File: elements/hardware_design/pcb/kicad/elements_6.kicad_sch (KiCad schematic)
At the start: 19 parts

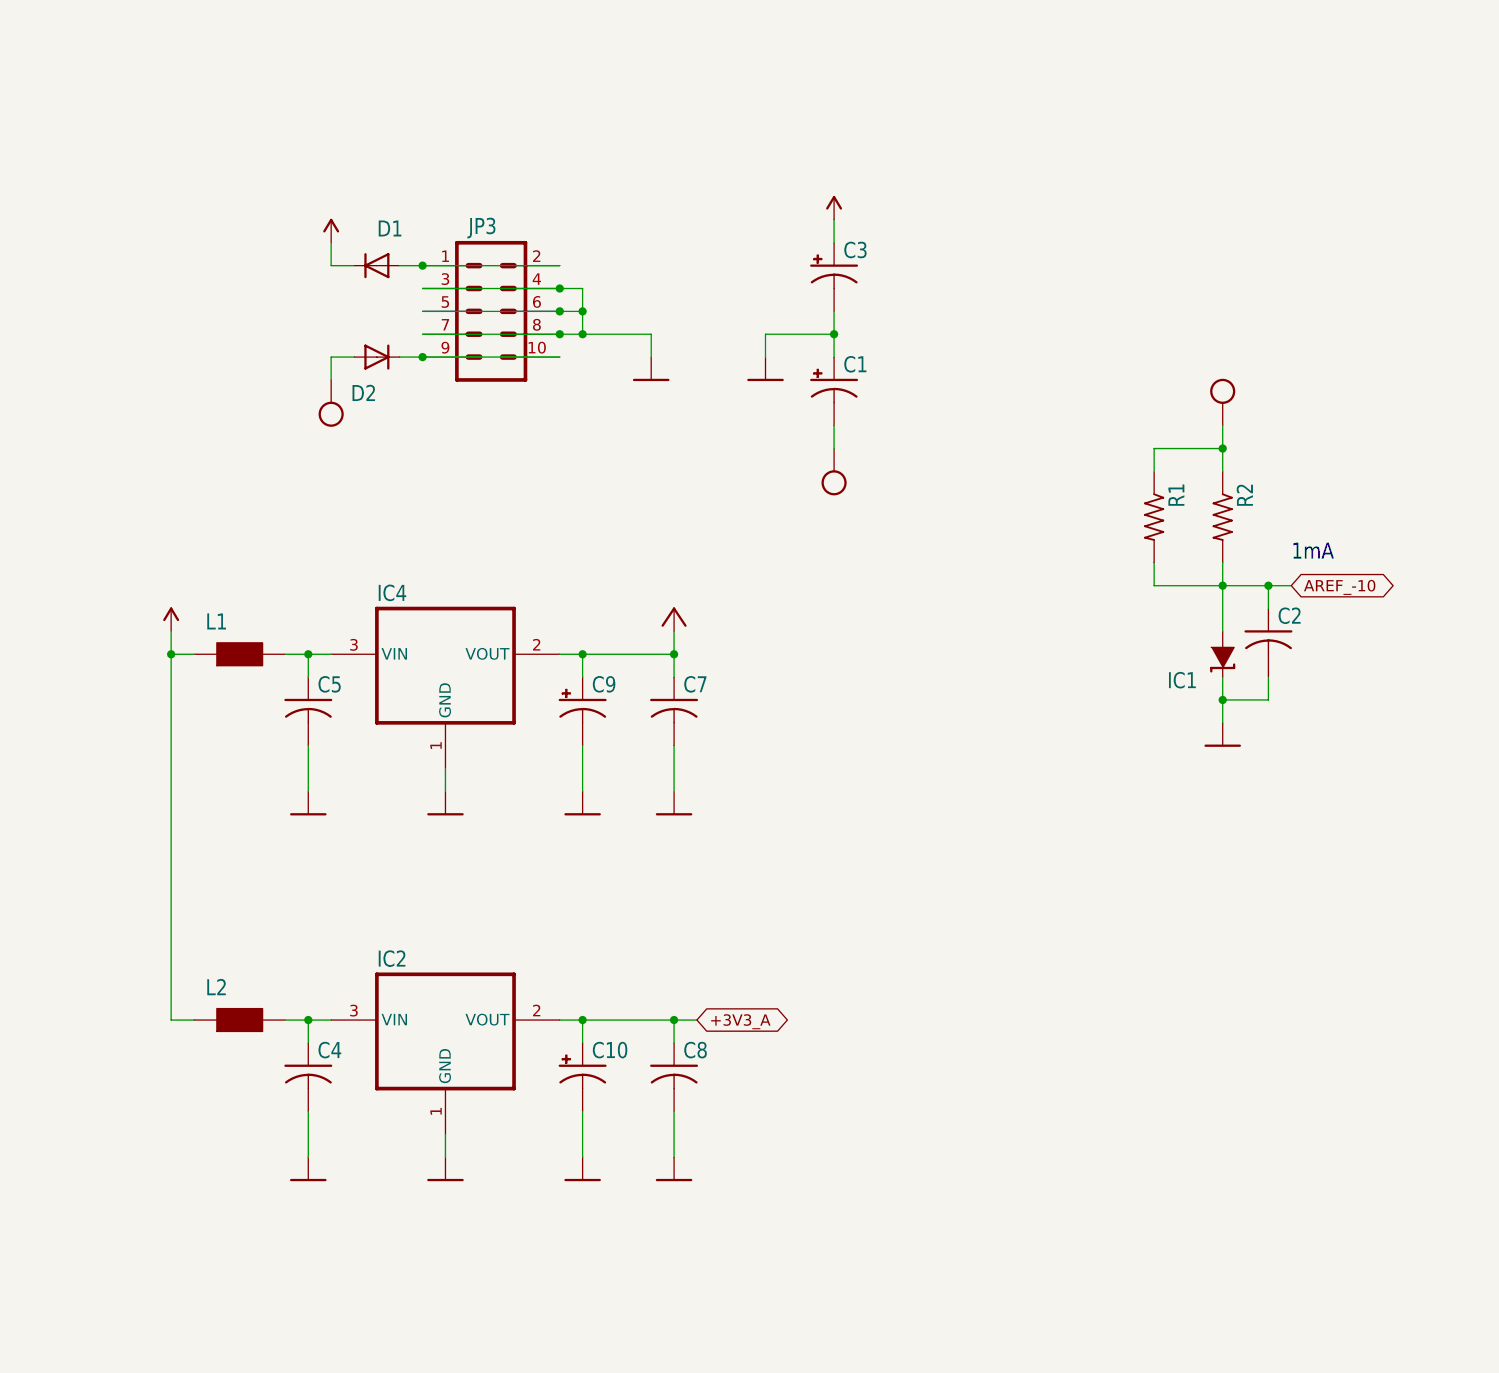
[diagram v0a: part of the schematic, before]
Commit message: swap wm8731 package (haven't drawn traces yet)
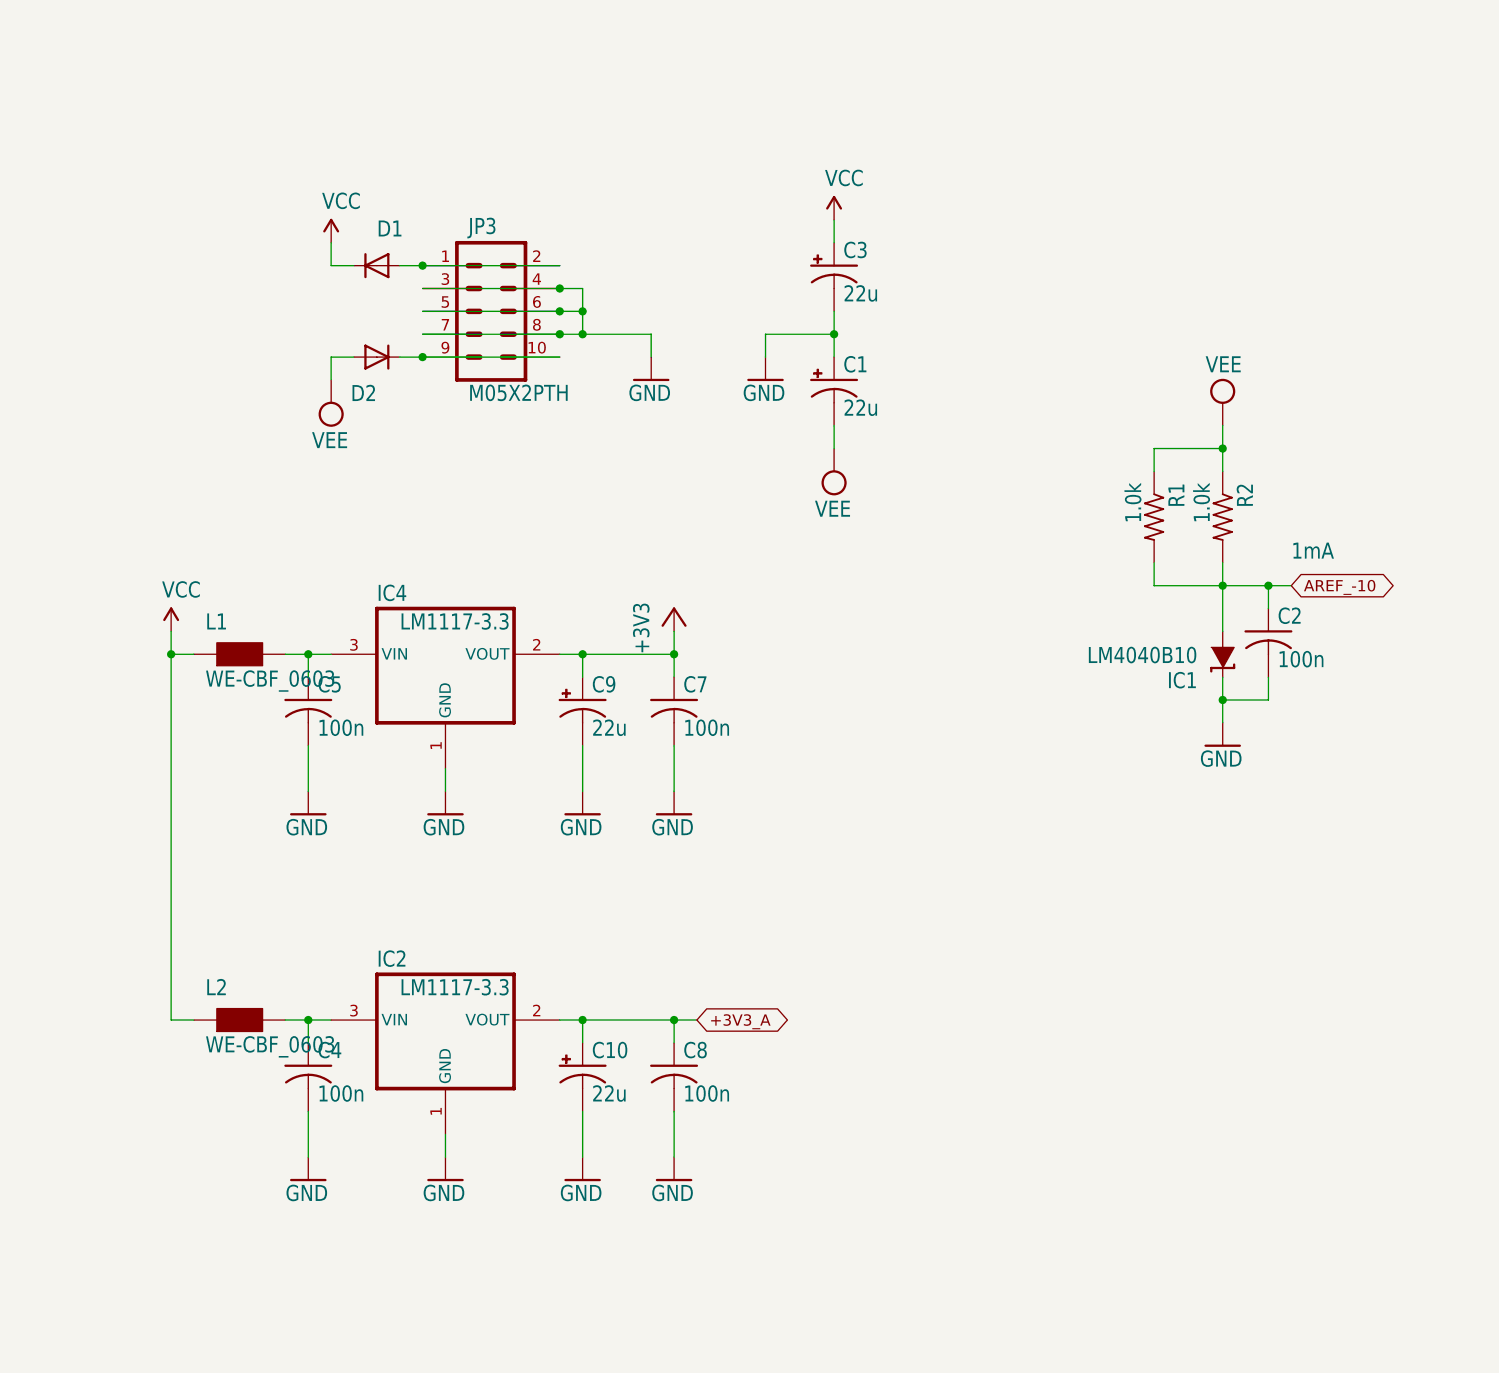
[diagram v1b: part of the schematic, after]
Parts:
- C1, C10, C3, C9: value (none) -> 22u; footprint (none) -> elements:PANASONIC_C
- C2, C4, C5, C7, C8: value (none) -> 100n; footprint (none) -> elements:C0603
- D1, D2: value (none) -> 1N5819HW; footprint (none) -> elements:SOD123
- IC1: value (none) -> LM4040B10; footprint (none) -> elements:DBZ_R-PDSO-G3
- IC2, IC4: value (none) -> LM1117-3.3; footprint (none) -> elements:SOT223
- JP3: value (none) -> M05X2PTH; footprint (none) -> elements:AVR_ICSP
- L1, L2: value (none) -> WE-CBF_0603; footprint (none) -> elements:0603
- R1, R2: value (none) -> 1.0k; footprint (none) -> elements:R0603

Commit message: add optional SMD power
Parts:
- added J19: Conn_02x05_Odd_Even, Connector_PinHeader_2.54mm:PinHeader_2x05_P2.54mm_Vertical_SMD, symbol Connector_Generic:Conn_02x05_Odd_Even
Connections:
- net GND: now also J19.3 (Pin_3), J19.4 (Pin_4), J19.5 (Pin_5), J19.6 (Pin_6), J19.7 (Pin_7), J19.8 (Pin_8)
- net at D2.C, JP3.10, JP3.9: now also J19.10 (Pin_10), J19.9 (Pin_9)
- net at D1.A, JP3.1, JP3.2: now also J19.1 (Pin_1), J19.2 (Pin_2)
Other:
- moved on the sheet: D1, D2, JP3
